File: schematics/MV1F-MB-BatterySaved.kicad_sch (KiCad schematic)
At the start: 11 parts, among them Q1 2SA1015, Q2 2SC1815, U2 74LS32

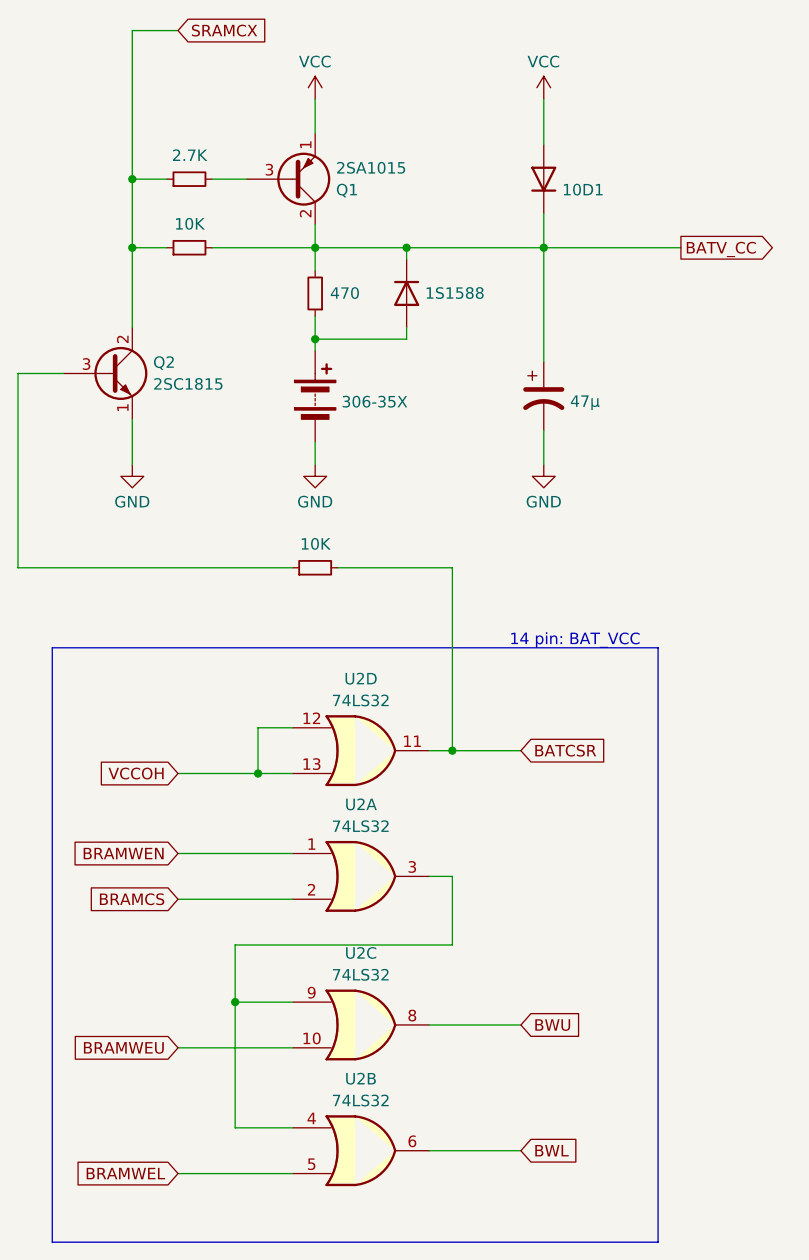
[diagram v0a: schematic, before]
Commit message: complete DaughterBoard
rename sub files
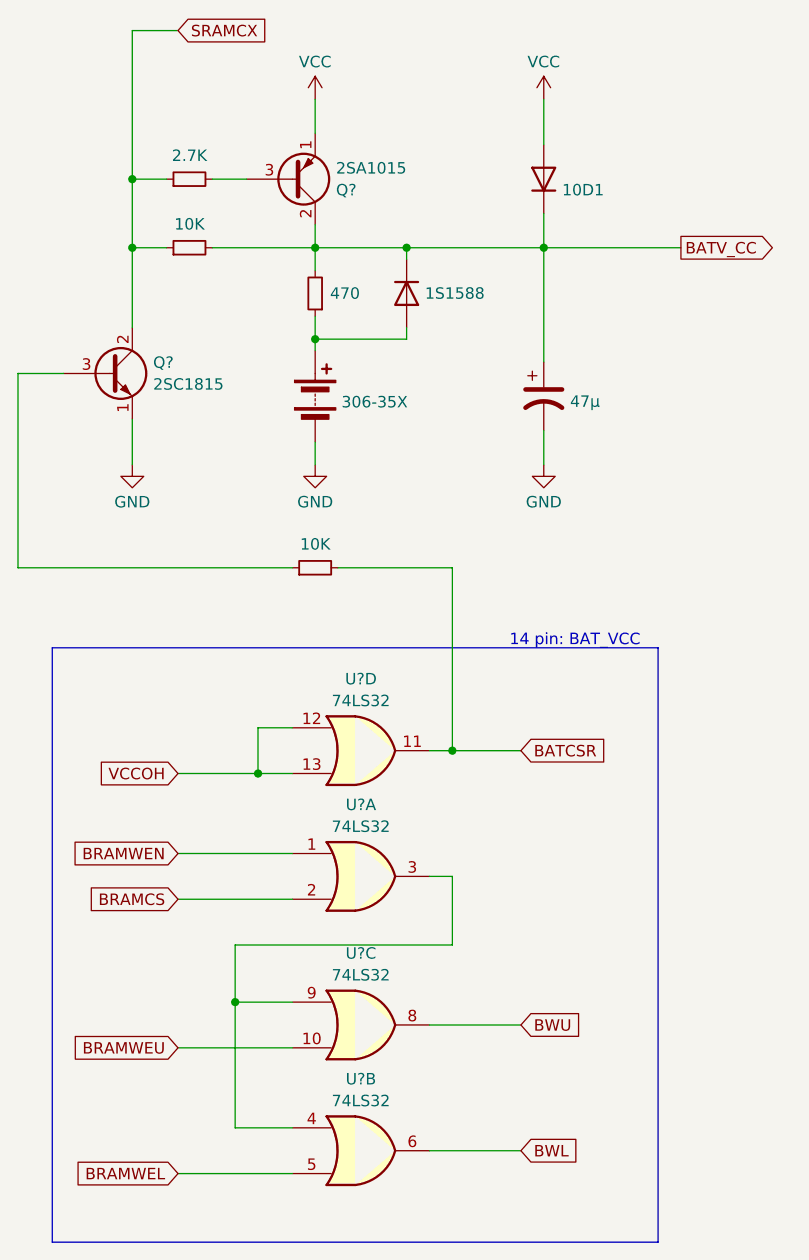
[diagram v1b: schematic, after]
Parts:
- renumbered BT1 to BT?, C1 to C?, D2 to D?, D1 to D?, Q2 to Q?, Q1 to Q?, R3 to R?, R4 to R?, R1 to R?, R2 to R?, U2 to U?

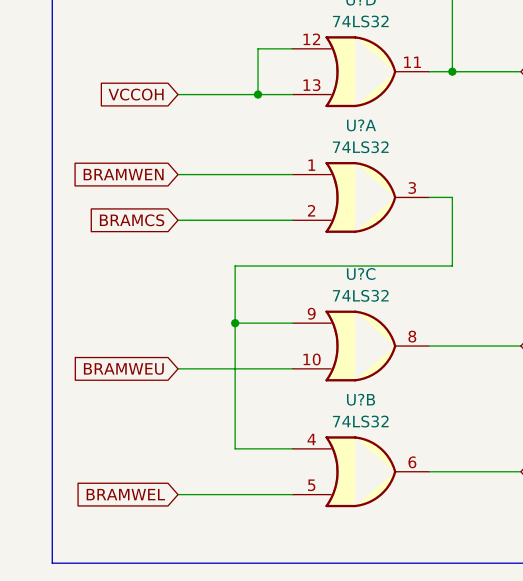
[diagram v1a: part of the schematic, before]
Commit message: Typo... and orphan labels remove
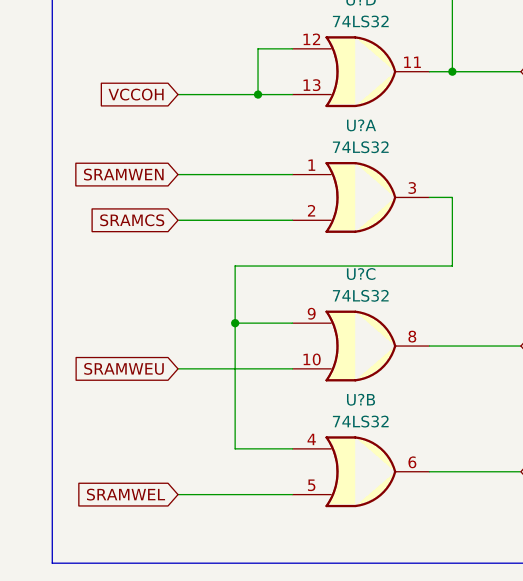
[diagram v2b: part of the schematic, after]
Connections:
- net BRAMCS renamed SRAMCS
- net BRAMWEL renamed SRAMWEL
- net BRAMWEN renamed SRAMWEN
- net BRAMWEU renamed SRAMWEU
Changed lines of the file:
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@@
     )
   )
-  (global_label "BRAMWEN" (shape input) (at 46.99 114.3 180) (fields_autoplaced)
+  (global_label "SRAMWEN" (shape input) (at 46.99 114.3 180) (fields_autoplaced)
     (effects (font (size 1.27 1.27)) (justify right))
     (property "Intersheetrefs" "${INTERSHEET_REFS}" (at 34.9939 114.3 0)
@@
     )
   )
-  (global_label "BRAMCS" (shape input) (at 46.99 119.38 180) (fields_autoplaced)
+  (global_label "SRAMCS" (shape input) (at 46.99 119.38 180) (fields_autoplaced)
     (effects (font (size 1.27 1.27)) (justify right))
     (property "Intersheetrefs" "${INTERSHEET_REFS}" (at 36.4453 119.38 0)
@@
     )
   )
-  (global_label "BRAMWEU" (shape input) (at 46.99 135.89 180) (fields_autoplaced)
+  (global_label "SRAMWEU" (shape input) (at 46.99 135.89 180) (fields_autoplaced)
     (effects (font (size 1.27 1.27)) (justify right))
     (property "Intersheetrefs" "${INTERSHEET_REFS}" (at 34.9939 135.89 0)
@@
     )
   )
-  (global_label "BRAMWEL" (shape input) (at 46.99 149.86 180) (fields_autoplaced)
+  (global_label "SRAMWEL" (shape input) (at 46.99 149.86 180) (fields_autoplaced)
     (effects (font (size 1.27 1.27)) (justify right))
     (property "Intersheetrefs" "${INTERSHEET_REFS}" (at 35.2963 149.86 0)

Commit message: Typo
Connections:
- net SRAMCX is gone; now on net BRAMCS: Q?.2 (C), R?.1, R?.1
- net BATV_CC renamed BAT_VCC
- net SRAMCS renamed BRAMCS
- net SRAMWEL renamed BRAMWEL
- net SRAMWEN renamed BRAMWEH
- net SRAMWEU renamed BRAMWEU
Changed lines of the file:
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@@
     (stroke (width 0) (type default))
   )
-  (wire (pts (xy 46.99 114.3) (xy 59.69 114.3))
+  (wire (pts (xy 48.26 114.3) (xy 59.69 114.3))
     (stroke (width 0) (type default))
   )
@@
     (stroke (width 0) (type default))
   )
-  (wire (pts (xy 46.99 119.38) (xy 59.69 119.38))
+  (wire (pts (xy 48.26 119.38) (xy 59.69 119.38))
     (stroke (width 0) (type default))
   )
@@
     (stroke (width 0) (type default))
   )
-  (wire (pts (xy 46.99 105.41) (xy 55.88 105.41))
+  (wire (pts (xy 48.26 105.41) (xy 55.88 105.41))
     (stroke (width 0) (type default))
   )
@@
     (stroke (width 0) (type default))
   )
-  (wire (pts (xy 46.99 149.86) (xy 59.69 149.86))
+  (wire (pts (xy 48.26 149.86) (xy 59.69 149.86))
     (stroke (width 0) (type default))
   )
@@
     (stroke (width 0) (type default))
   )
-  (wire (pts (xy 46.99 135.89) (xy 59.69 135.89))
+  (wire (pts (xy 48.26 135.89) (xy 59.69 135.89))
     (stroke (width 0) (type default))
   )
@@
     )
   )
-  (global_label "SRAMWEN" (shape input) (at 46.99 114.3 180) (fields_autoplaced)
+  (global_label "BRAMWEH" (shape input) (at 48.26 114.3 180) (fields_autoplaced)
     (effects (font (size 1.27 1.27)) (justify right))
-    (property "Intersheetrefs" "${INTERSHEET_REFS}" (at 34.9939 114.3 0)
+    (property "Intersheetrefs" "${INTERSHEET_REFS}" (at 36.2639 114.3 0)
       (effects (font (size 1.27 1.27)) (justify right))
     )
   )
-  (global_label "SRAMCS" (shape input) (at 46.99 119.38 180) (fields_autoplaced)
+  (global_label "BRAMCS" (shape input) (at 48.26 119.38 180) (fields_autoplaced)
     (effects (font (size 1.27 1.27)) (justify right))
-    (property "Intersheetrefs" "${INTERSHEET_REFS}" (at 36.4453 119.38 0)
+    (property "Intersheetrefs" "${INTERSHEET_REFS}" (at 37.7153 119.38 0)
       (effects (font (size 1.27 1.27)) (justify right))
     )
   )
-  (global_label "SRAMCX" (shape input) (at 46.99 22.86 0) (fields_autoplaced)
+  (global_label "BRAMCS" (shape input) (at 46.99 22.86 0) (fields_autoplaced)
     (effects (font (size 1.27 1.27)) (justify left))
-    (property "Intersheetrefs" "${INTERSHEET_REFS}" (at 57.4742 22.86 0)
+    (property "Intersheetrefs" "${INTERSHEET_REFS}" (at 57.5347 22.86 0)
       (effects (font (size 1.27 1.27)) (justify left))
     )
@@
     )
   )
-  (global_label "SRAMWEU" (shape input) (at 46.99 135.89 180) (fields_autoplaced)
+  (global_label "BRAMWEU" (shape input) (at 48.26 135.89 180) (fields_autoplaced)
     (effects (font (size 1.27 1.27)) (justify right))
-    (property "Intersheetrefs" "${INTERSHEET_REFS}" (at 34.9939 135.89 0)
+    (property "Intersheetrefs" "${INTERSHEET_REFS}" (at 36.2639 135.89 0)
       (effects (font (size 1.27 1.27)) (justify right))
     )
   )
-  (global_label "VCCOH" (shape input) (at 46.99 105.41 180) (fields_autoplaced)
+  (global_label "VCCOH" (shape input) (at 48.26 105.41 180) (fields_autoplaced)
     (effects (font (size 1.27 1.27)) (justify right))
-    (property "Intersheetrefs" "${INTERSHEET_REFS}" (at 37.7152 105.41 0)
+    (property "Intersheetrefs" "${INTERSHEET_REFS}" (at 38.9852 105.41 0)
       (effects (font (size 1.27 1.27)) (justify right))
     )
   )
-  (global_label "SRAMWEL" (shape input) (at 46.99 149.86 180) (fields_autoplaced)
+  (global_label "BRAMWEL" (shape input) (at 48.26 149.86 180) (fields_autoplaced)
     (effects (font (size 1.27 1.27)) (justify right))
-    (property "Intersheetrefs" "${INTERSHEET_REFS}" (at 35.2963 149.86 0)
+    (property "Intersheetrefs" "${INTERSHEET_REFS}" (at 36.5663 149.86 0)
       (effects (font (size 1.27 1.27)) (justify right))
     )
   )
-  (global_label "BATV_CC" (shape output) (at 102.87 46.99 0) (fields_autoplaced)
+  (global_label "BAT_VCC" (shape input) (at 102.87 46.99 0) (fields_autoplaced)
     (effects (font (size 1.27 1.27)) (justify left))
     (property "Intersheetrefs" "${INTERSHEET_REFS}" (at 113.7776 46.99 0)
